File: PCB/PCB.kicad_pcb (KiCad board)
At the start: 2 copper layers, 143.2 x 113.5 mm, 78 parts, among them SW10 SW_Push, SW11 SW_Push, SW12 SW_Push, SW13 SW_Push, SW14 SW_Push, SW15 SW_Push, SW16 SW_Push, SW17 SW_Push, SW18 SW_Push, SW19 SW_Push, SW2 SW_Push, SW20 SW_Push, SW21 SW_Push, SW22 SW_Push, SW23 SW_Push, SW24 SW_Push, SW25 SW_Push, SW26 SW_Push, SW3 SW_Push, SW4 SW_Push, SW5 SW_Push, SW6 SW_Push, SW7 SW_Push, SW8 SW_Push, SW9 SW_Push, U1 COM-09032, U2 COM-09032

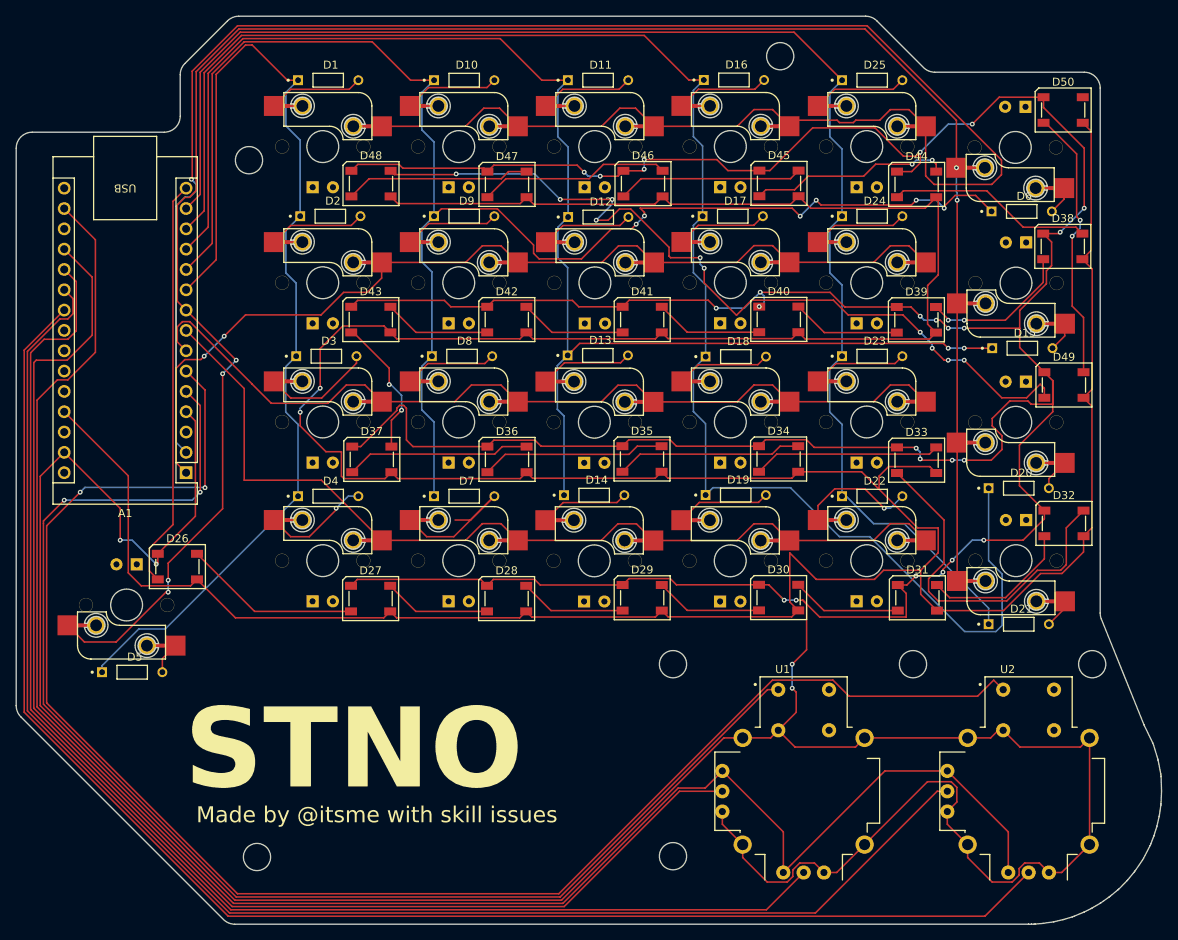
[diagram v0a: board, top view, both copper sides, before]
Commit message: fix the joystick footprint
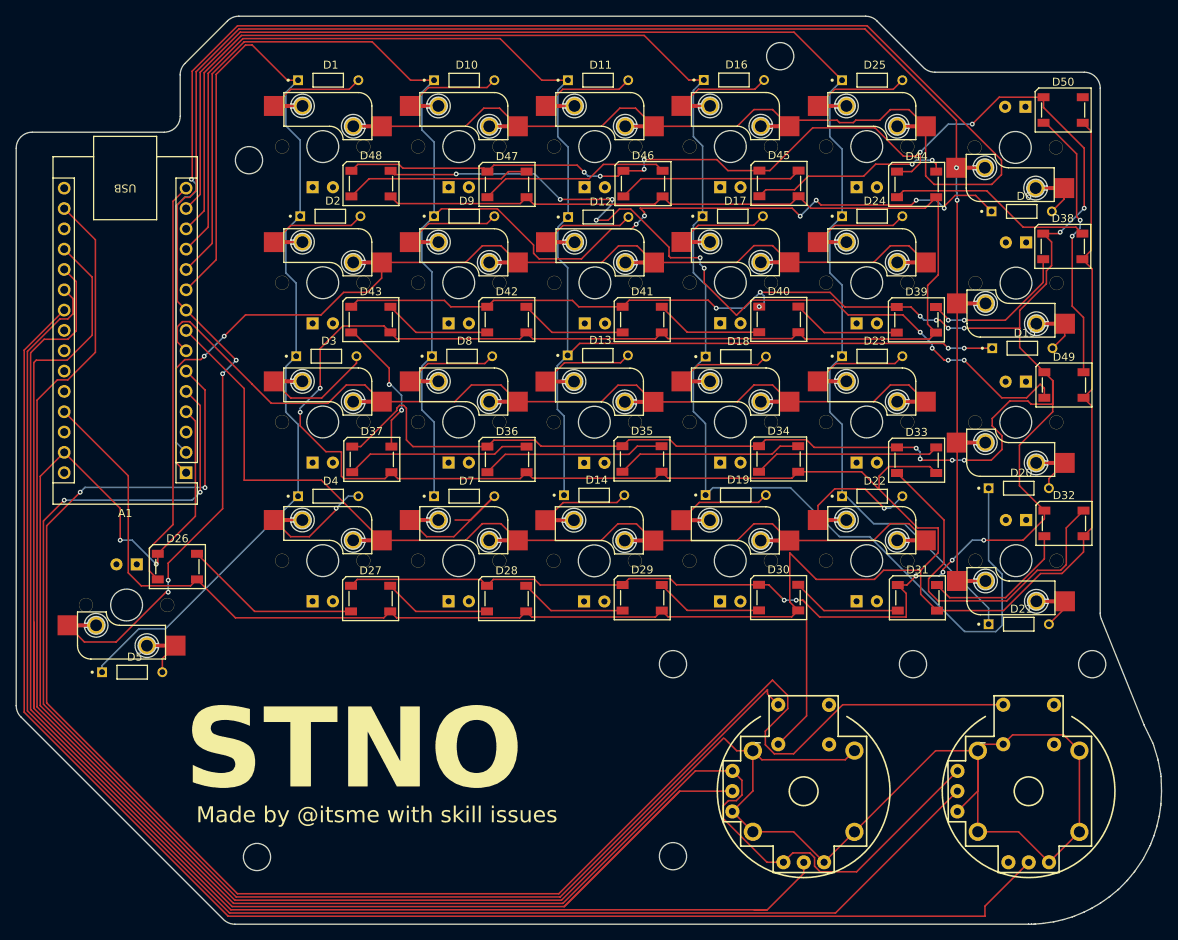
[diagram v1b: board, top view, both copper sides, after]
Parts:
- U1, U2: footprint stno:XDCR_COM-09032 -> stno:PS4_joystick
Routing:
- net V1: track 166.4 -> 198.8 mm
- net SEL2: track 202.2 -> 213.9 mm
- net +3V3: track 227.9 -> 218.5 mm
- net GND: track 796.5 -> 787.9 mm, vias 29 -> 27
- net H1: track 168.7 -> 171.5 mm
- net H2: track 190.7 -> 192.0 mm
- net V2: track 187.8 -> 189.0 mm
- net SEL1: track 169.9 -> 171.0 mm

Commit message: put all the hotswap switches on the right side
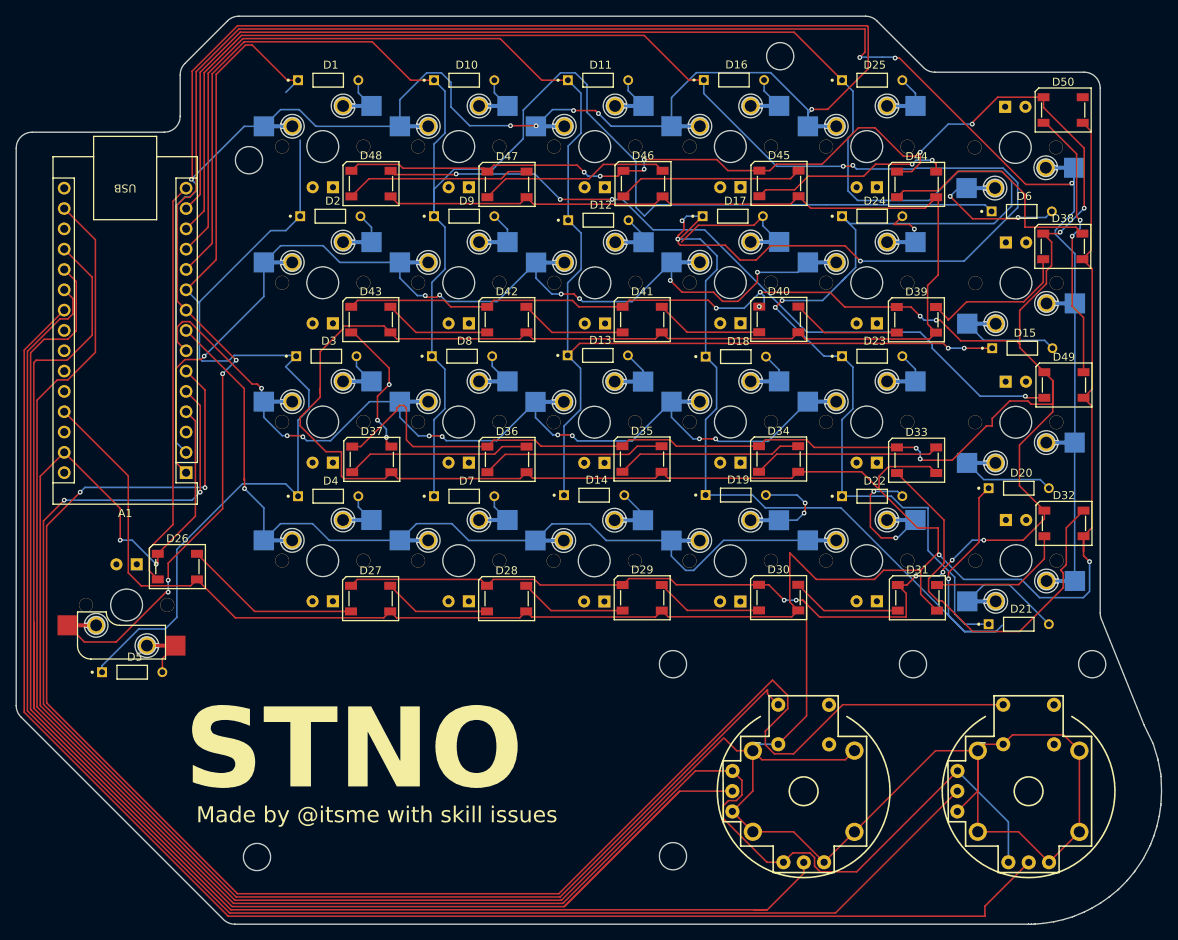
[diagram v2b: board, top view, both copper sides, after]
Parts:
- SW10, SW11, SW12, SW13, SW14, SW15, SW16, SW17, SW18, SW19, SW2, SW20, SW21, SW22, SW23, SW24, SW25, SW26, SW3, SW4, SW5, SW7, SW8, SW9: moved to B.Cu
- moved D12 0.39 mm to (128.3, 55.5)
- turned SW10 to 180 degrees
- turned SW11 to 0 degrees
- turned SW12 to 180 degrees
- turned SW13 to 180 degrees
- turned SW14 to 180 degrees
- turned SW15 to 180 degrees
- turned SW16 to 180 degrees
- turned SW17 to 180 degrees
- turned SW18 to 180 degrees
- turned SW19 to 180 degrees
- turned SW2 to 180 degrees
- turned SW20 to 0 degrees
- turned SW21 to 0 degrees
- turned SW22 to 180 degrees
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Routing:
- net Row 4: track 205.5 -> 300.3 mm, vias 0 -> 6
- net Row 5: track 184.5 -> 245.9 mm, vias 0 -> 2
- net Row 1: track 132.0 -> 152.9 mm
- net Column 5: track 248.6 -> 267.5 mm, vias 6 -> 7
- net Net-(D7-PadA): track 19.6 -> 3.66 mm
- net +3V3: track 218.5 -> 232.6 mm
- net Row 2: track 193.8 -> 207.7 mm, vias 6 -> 0
- net Net-(D6-PadA): track 3.55 -> 16.7 mm, vias 0 -> 2
- net Net-(D48-DOUT): track 105.2 -> 93.8 mm, vias 10 -> 4
- net Net-(D4-PadA): track 13.6 -> 3.66 mm, vias 1 -> 0
- net Net-(D3-PadA): track 13.9 -> 3.92 mm
- net Net-(D21-PadA): track 3.68 -> 13.1 mm
- net Column 4: track 116.9 -> 107.9 mm, vias 0 -> 1
- net Net-(D15-PadA): track 3.69 -> 12.4 mm
- net Net-(D2-PadA): track 12.1 -> 3.81 mm
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
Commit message: hotswap switches fixed
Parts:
- SW10, SW11, SW12, SW13, SW14, SW15, SW16, SW17, SW18, SW19, SW2, SW20, SW21, SW22, SW23, SW24, SW25, SW26, SW3, SW4, SW5, SW6, SW7, SW8, SW9: footprint keebio:Kailh_MX_Socket-compat -> Library:hotswap

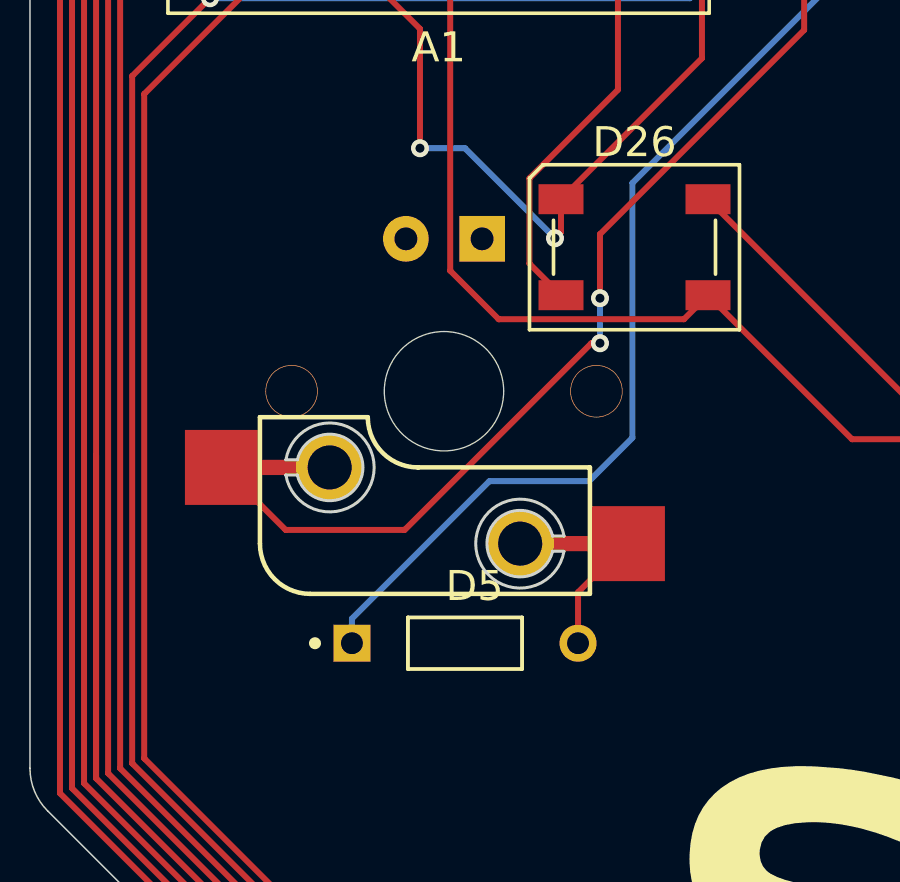
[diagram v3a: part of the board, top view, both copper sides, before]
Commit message: ajouter des empreintes pour les touches, les diodes, et le microcontrôleur
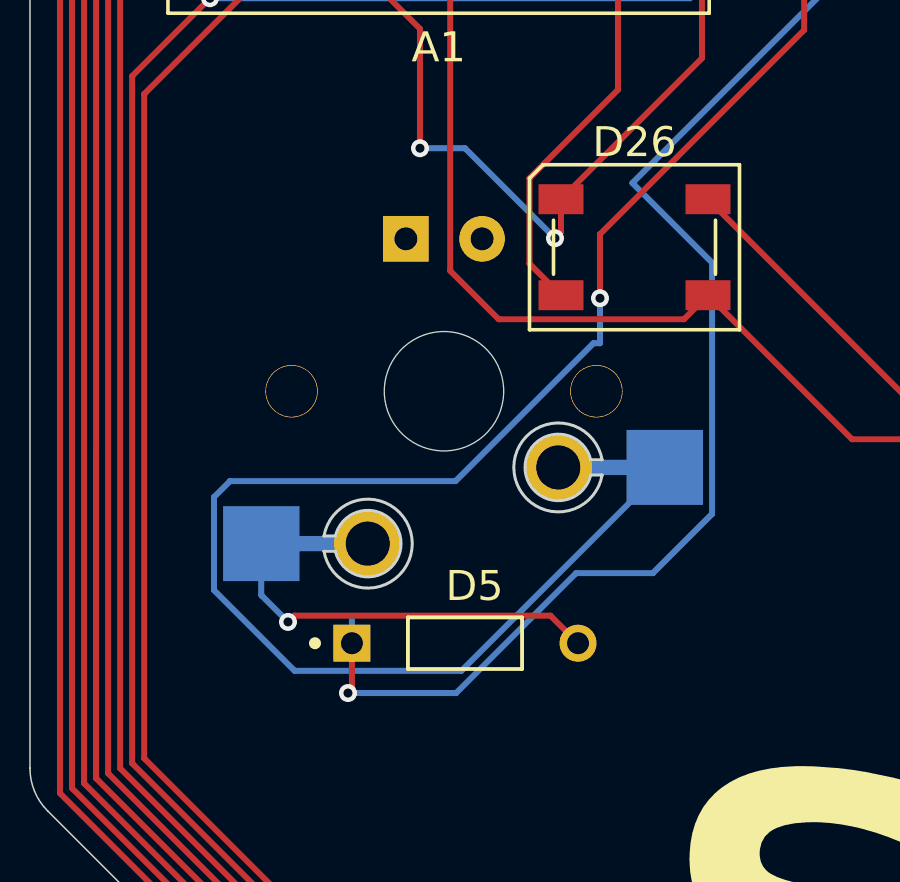
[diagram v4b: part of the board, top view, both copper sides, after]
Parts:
- SW6: moved to B.Cu
- turned SW6 to 0 degrees
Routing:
- net Column 5: track 267.5 -> 288.5 mm, vias 7 -> 6
- net Net-(D5-PadA): track 3.99 -> 13.1 mm, vias 0 -> 1
- net Row 1: track 152.9 -> 161.0 mm, vias 0 -> 1

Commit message: quickly made journal entry
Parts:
- added G***: LOGO, LOGO, F.Cu at (133.4, 116.1)
